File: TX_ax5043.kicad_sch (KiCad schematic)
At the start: 27 parts, among them P6 CONUFL001-SMD-T, P7 CONUFL001-SMD-T, Q7 DMP2160UWQ-7, U23 AX5043

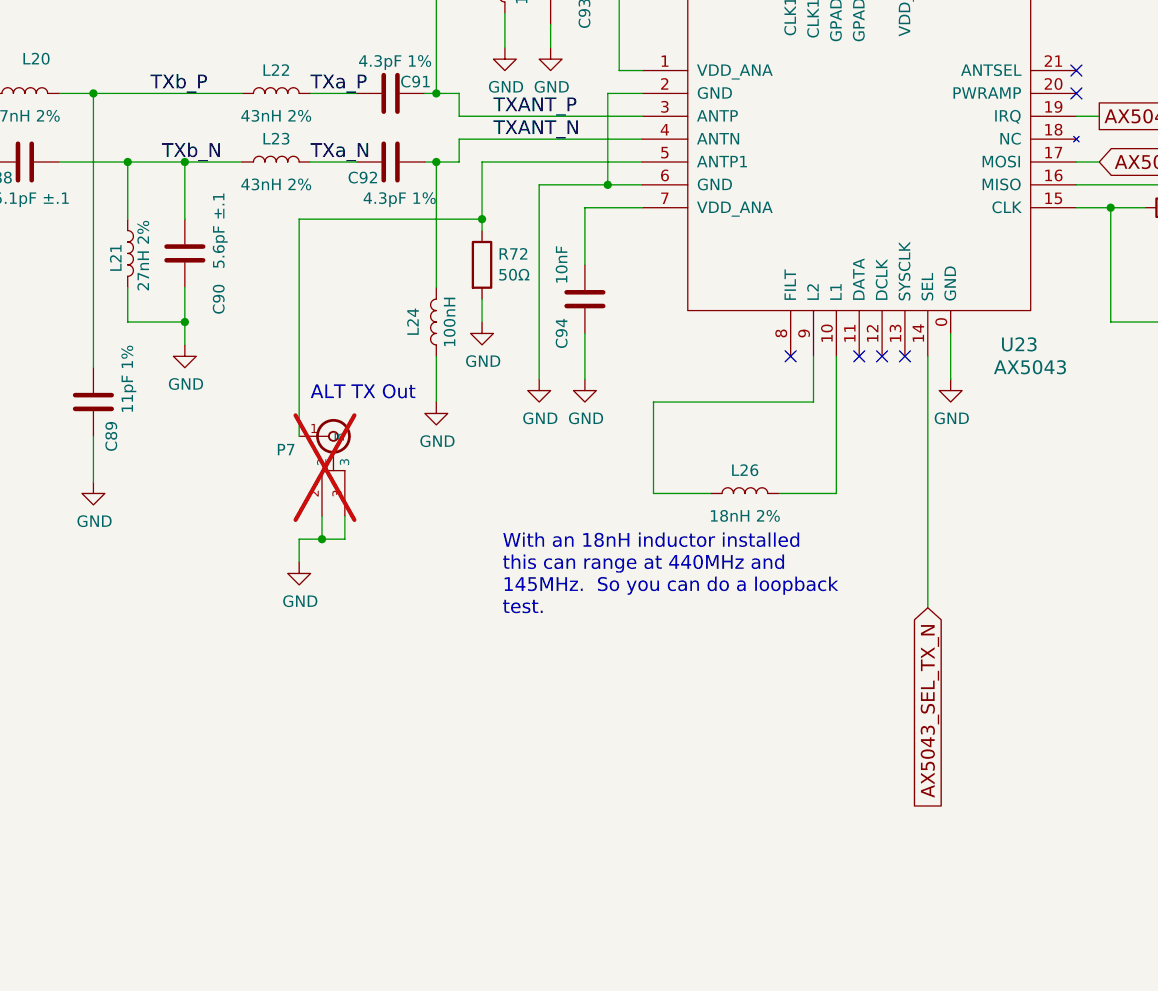
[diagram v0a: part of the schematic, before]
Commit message: Add a U.FL connector to ANTP1 on AX5043 RX4
Add it with a matching network, and add a matching network on the one on
the TX AX5043, too.  All DNP.

Signed-off-by: Corey Minyard <corey@minyard.net>
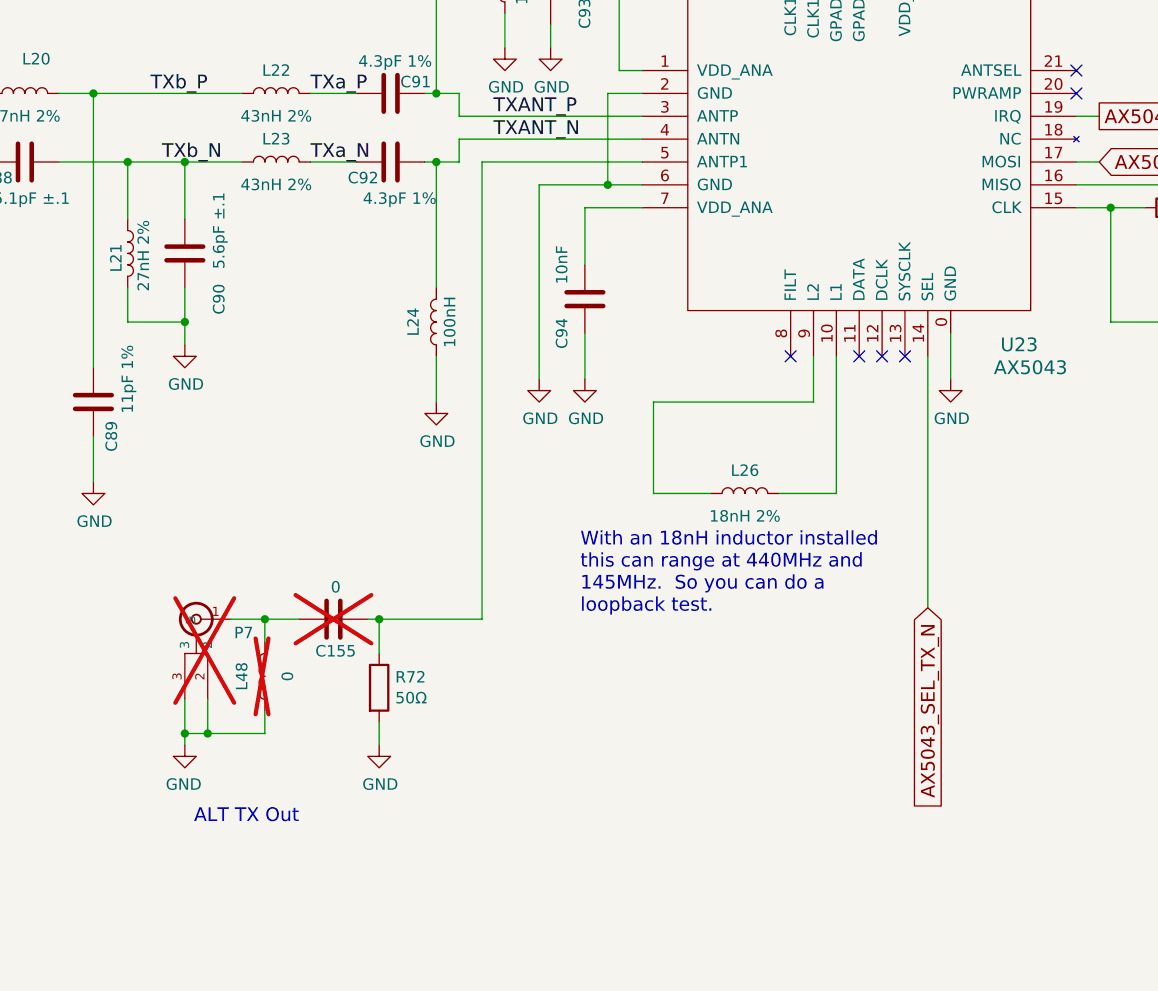
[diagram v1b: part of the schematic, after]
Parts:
- added C155: 0, Capacitor_SMD:C_0402_1005Metric_Pad0.74x0.62mm_HandSolder, symbol Device:C
- added L48: 0, Inductor_SMD:L_0402_1005Metric_Pad0.77x0.64mm_HandSolder, symbol Device:L
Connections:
- net GND: now also L48.1
- net at R72.1, U23.5 (ANTP1): now also C155.1; no longer P7.1 (In)
- new net: C155.2, L48.2, P7.1 (In)
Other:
- moved on the sheet: P7, R72
